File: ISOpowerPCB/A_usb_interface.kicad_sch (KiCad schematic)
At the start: 19 parts

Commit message: modified pcb files
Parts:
- removed C? (x2): 100n, Capacitor_SMD:C_0805_2012Metric_Pad1.18x1.45mm_HandSolder, symbol 000_Capacitor_film_immo:cap_film_0805
- removed C?: 4n7, Capacitor_SMD:C_0805_2012Metric_Pad1.18x1.45mm_HandSolder, symbol 000_Capacitor_film_immo:cap_film_0805
- removed D?: PRTR5V0U2X, Package_TO_SOT_SMD:SOT-143, symbol Power_Protection:PRTR5V0U2X
- removed J?: USB_B_Mini, symbol Connector:USB_B_Mini
- removed R?: 1M, Resistor_SMD:R_0805_2012Metric_Pad1.20x1.40mm_HandSolder, symbol 000_Resistors_Immo:Resistor_0805
- removed TP? (x2): TestPoint, symbol Connector:TestPoint
- removed U?: CH340C, Package_SO:SOIC-16_3.9x9.9mm_P1.27mm, symbol Interface_USB:CH340C
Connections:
- no-connect marks 2 -> 1
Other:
- moved on the sheet: C?, D?, J?, R?, TP?, U?

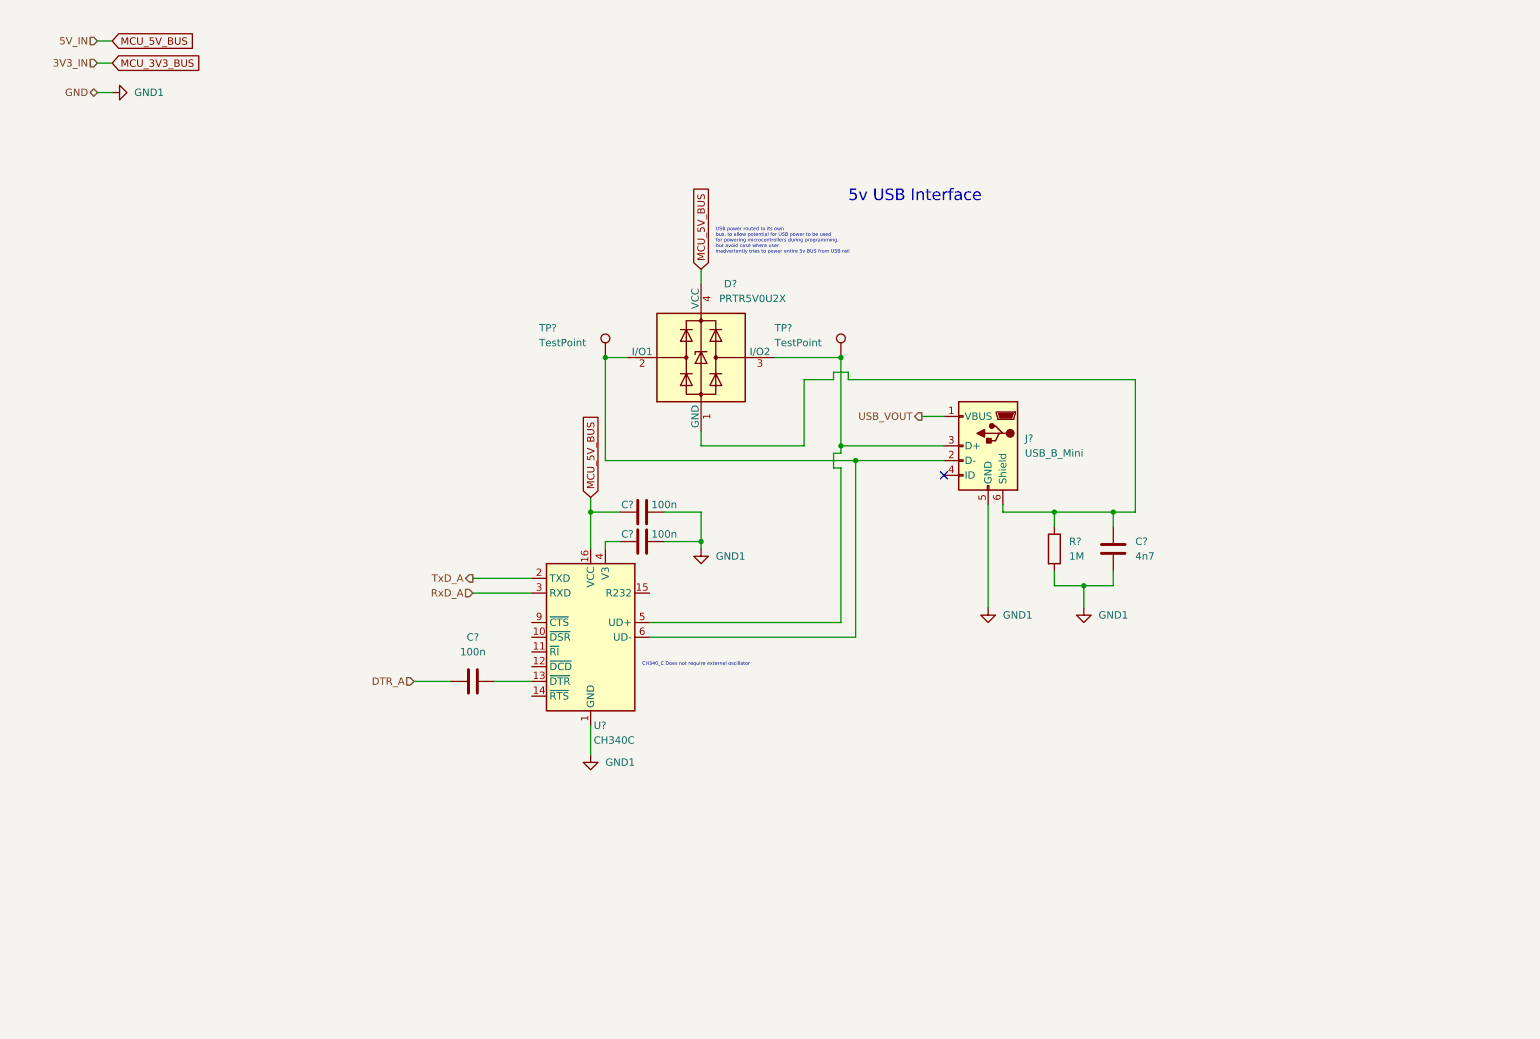
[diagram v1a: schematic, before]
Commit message: Finished initial circuit design
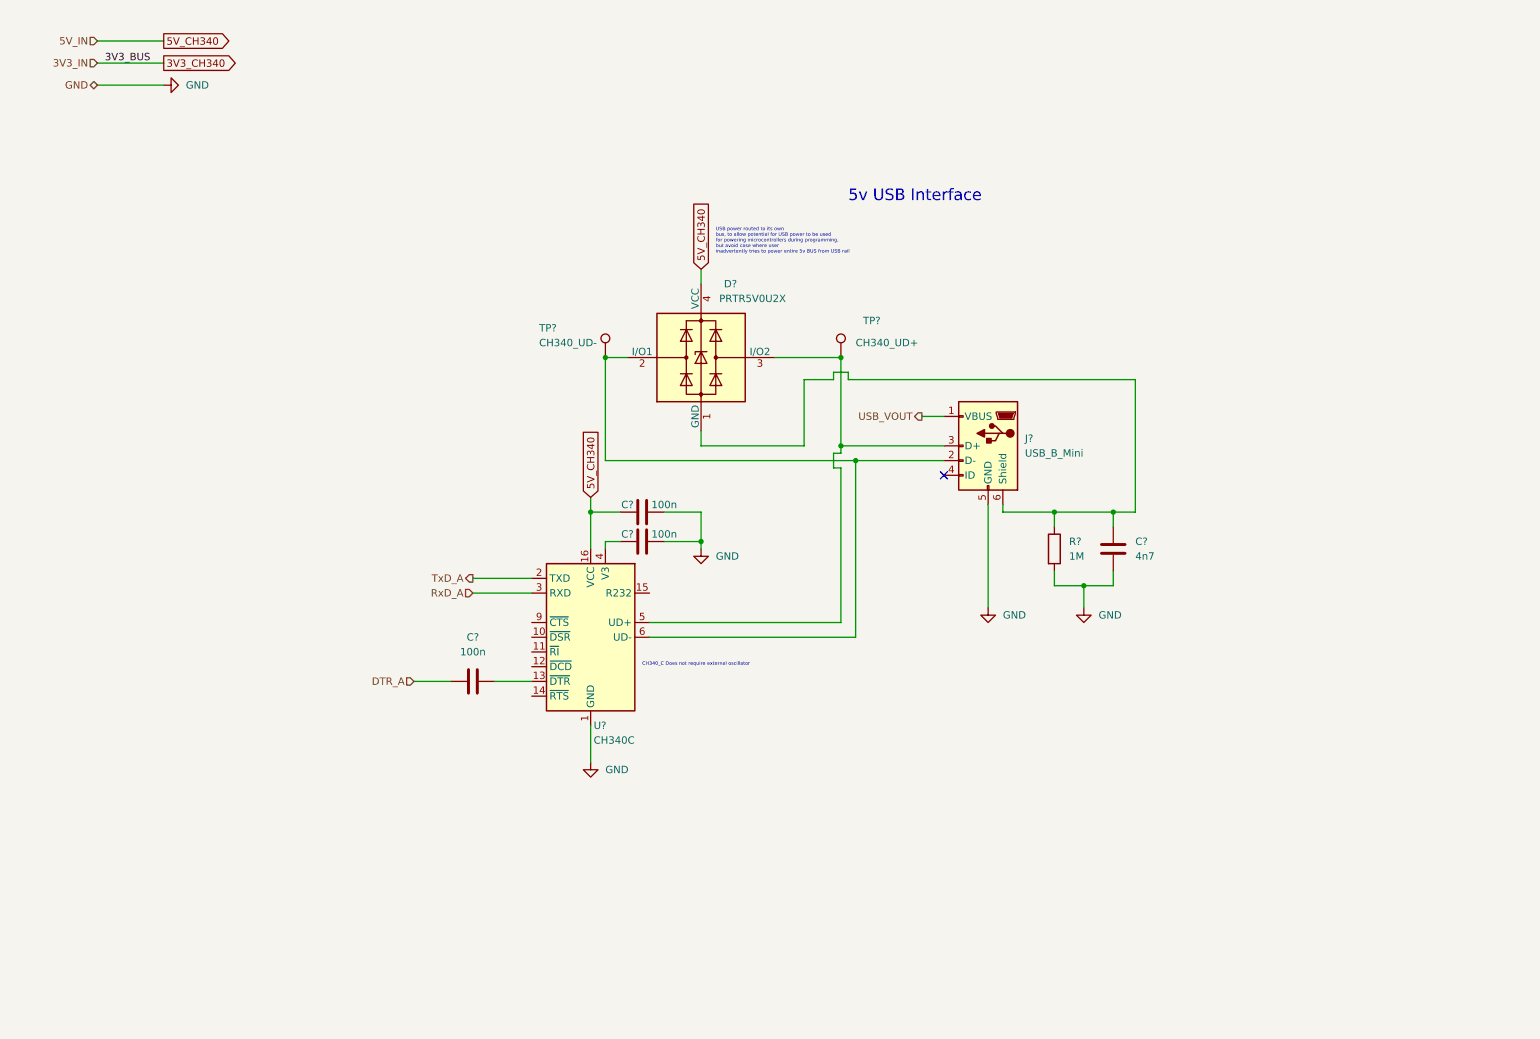
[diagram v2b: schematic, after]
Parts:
- TP?: value TestPoint -> CH340_UD+
- TP?: value TestPoint -> CH340_UD-
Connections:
- net GND1 renamed GND
- net MCU_5V_BUS renamed 5V_CH340

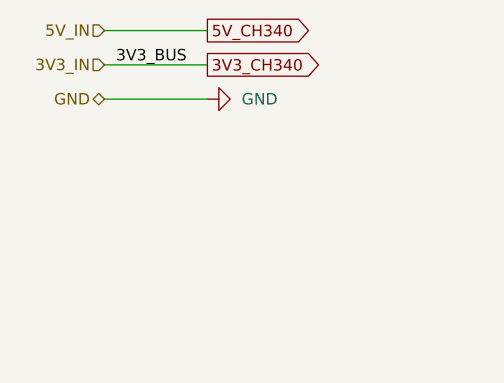
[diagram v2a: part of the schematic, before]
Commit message: Updated as per discussions 26/01/22
# Change Notes

04/02/2022
As per discussion 26/01/22
1. Changed per channel 5v MOSFET switches to MOSFET control of DC/DC module on/off pin - due to failure of MOSFET switching during testing.
2. Added 5v buck converter for independent MCU_5V power bus.
	- Ensured all 5v MCU hardware is powered from common MCU_5V bus.
3. Removed circuit from NC pins on DC/DC modules.
4. Changed ESP32 USB interface to CH340
5. Changed MCU serial logic level converters from MOSFET to IC - TXS0102DCT
	- TODO: OE pin now requires low signal untill DC/DC supply is stable - Does it? Can it just be tied to 5v bus with a large capacitor? Does it need MCU to hold pin low untill 5V_BUS is stable?
6. Removed redundent 3V3_IN to power distribution page.
	- Rechecked all sheets for redundent pins, it won't impact drawing traces, but it will impact readability.
7. Added Mechanical layer as hirarchical sheet.
8. Moved voltage monitoring circuits to hirarchical sheet
9. Added voltage monitoring with TL431DBZ to 12V_BUS
10. Automatic shutoff circuit removed, as this would prevent the DC/DC module from powering on. Instead moved to AtMega328p digital inputs
and microcontroller will control shutdown of DC/DC supply if out of spec voltage detected.
		- This is a severe limitation compared to the specification, and this also does not prevent damage to devices on 5V_BUS if voltage is pulled high, for example to 12v due to user error.
		- TODO: Add independent overvoltage protection to 5V_BUS? 		[Zener Diode Overvoltage Protection - Sparkfun](https://www.rs-online.com/designspark/how-does-zener-diode-do-overvoltage-protection-in-circuit#:~:text=In%20order%20to%20protect%20the,flow%20in%20the%20reverse%20direction).
11. Changed logic level conversion for 12v outputs to 12v drive circuit. [12v drive circuit](https://forum.arduino.cc/t/easiest-way-of-driving-amplifying-from-5v-to-12v/123290)
12. Added proto pin connections for ESP MCU.
13. Changed 20v Zener in reverse vol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
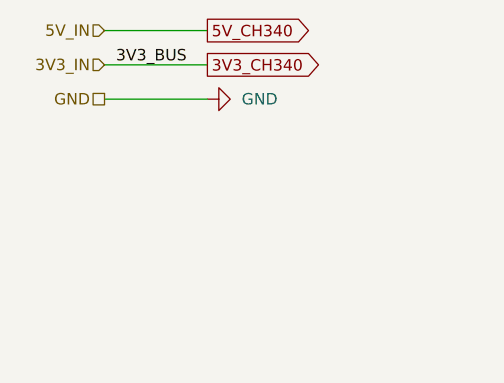
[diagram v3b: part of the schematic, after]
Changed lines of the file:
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@@
     (effects (font (size 1.27 1.27)) (justify right))
   )
-  (hierarchical_label "GND" (shape bidirectional) (at 27.94 30.48 180)
+  (hierarchical_label "GND" (shape passive) (at 27.94 30.48 180)
     (effects (font (size 1.27 1.27)) (justify right))
   )

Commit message: messing around with libraries
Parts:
- C22, C23, C24, C25: renamed from C?; symbol 000_Capacitor_film_immo:cap_film_0805 -> 000_Capacitor_FIlm_Immo:cap_film_0805
- gave numbers to parts that had none: 6
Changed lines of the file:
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@@
     (effects (font (size 1.27 1.27)) (justify right))
   )
-  (symbol (lib_id "000_Capacitor_film_immo:cap_film_0805") (at 92.71 133.35 90) (unit 1)
-    (in_bom yes) (on_board yes) (fields_autoplaced)
-    (property "Reference" "C?" (id 0) (at 92.71 125.73 90))
+  (symbol (lib_id "000_Capacitor_FIlm_Immo:cap_film_0805") (at 92.71 133.35 90) (unit 1)
+    (in_bom yes) (on_board yes) (fields_autoplaced)
+    (property "Reference" "C22" (id 0) (at 92.71 125.73 90))
     (property "Value" "100n" (id 1) (at 92.71 128.27 90))
     (property "Footprint" "Capacitor_SMD:C_0805_2012Metric_Pad1.18x1.45mm_HandSolder" (id 2) (at 102.87 132.08 0)
@@
   (symbol (lib_id "power:GND") (at 181.61 120.65 0) (unit 1)
     (in_bom yes) (on_board yes) (fields_autoplaced)
-    (property "Reference" "#PWR?" (id 0) (at 181.61 127 0)
+    (property "Reference" "#PWR072" (id 0) (at 181.61 127 0)
       (effects (font (size 1.27 1.27)) hide)
     )
@@
     (pin "1")
   )
-  (symbol (lib_id "000_Capacitor_film_immo:cap_film_0805") (at 121.92 109.22 90) (unit 1)
-    (in_bom yes) (on_board yes)
-    (property "Reference" "C?" (id 0) (at 119.38 107.95 90))
+  (symbol (lib_id "000_Capacitor_FIlm_Immo:cap_film_0805") (at 121.92 109.22 90) (unit 1)
+    (in_bom yes) (on_board yes)
+    (property "Reference" "C24" (id 0) (at 119.38 107.95 90))
     (property "Value" "100n" (id 1) (at 125.73 107.95 90))
     (property "Footprint" "Capacitor_SMD:C_0805_2012Metric_Pad1.18x1.45mm_HandSolder" (id 2) (at 132.08 107.95 0)
@@
   (symbol (lib_id "Connector:TestPoint") (at 156.21 77.47 0) (unit 1)
     (in_bom yes) (on_board yes)
-    (property "Reference" "TP?" (id 0) (at 160.02 71.12 0)
+    (property "Reference" "TP8" (id 0) (at 160.02 71.12 0)
       (effects (font (size 1.27 1.27)) (justify left))
     )
@@
   (symbol (lib_id "Power_Protection:PRTR5V0U2X") (at 132.08 77.47 0) (unit 1)
     (in_bom yes) (on_board yes)
-    (property "Reference" "D?" (id 0) (at 137.16 64.77 0))
+    (property "Reference" "D4" (id 0) (at 137.16 64.77 0))
     (property "Value" "PRTR5V0U2X" (id 1) (at 140.97 67.31 0))
     (property "Footprint" "Package_TO_SOT_SMD:SOT-143" (id 2) (at 133.604 77.47 0)
@@
   (symbol (lib_id "power:GND") (at 113.03 147.32 0) (unit 1)
     (in_bom yes) (on_board yes) (fields_autoplaced)
-    (property "Reference" "#PWR?" (id 0) (at 113.03 153.67 0)
+    (property "Reference" "#PWR070" (id 0) (at 113.03 153.67 0)
       (effects (font (size 1.27 1.27)) hide)
     )
@@
   (symbol (lib_id "power:GND") (at 198.12 120.65 0) (unit 1)
     (in_bom yes) (on_board yes) (fields_autoplaced)
-    (property "Reference" "#PWR?" (id 0) (at 198.12 127 0)
+    (property "Reference" "#PWR073" (id 0) (at 198.12 127 0)
       (effects (font (size 1.27 1.27)) hide)
     )
@@
   (symbol (lib_id "000_Resistors_Immo:Resistor_0805") (at 193.04 110.49 0) (unit 1)
     (in_bom yes) (on_board yes)
-    (property "Reference" "R?" (id 0) (at 195.58 109.2199 0)
+    (property "Reference" "R8" (id 0) (at 195.58 109.2199 0)
       (effects (font (size 1.27 1.27)) (justify left))
     )
@@
   (symbol (lib_id "power:GND") (at 132.08 110.49 0) (unit 1)
     (in_bom yes) (on_board yes) (fields_autoplaced)
-    (property "Reference" "#PWR?" (id 0) (at 132.08 116.84 0)
+    (property "Reference" "#PWR071" (id 0) (at 132.08 116.84 0)
       (effects (font (size 1.27 1.27)) hide)
     )
@@
   (symbol (lib_id "Connector:TestPoint") (at 115.57 77.47 0) (unit 1)
     (in_bom yes) (on_board yes)
-    (property "Reference" "TP?" (id 0) (at 104.14 72.39 0)
+    (property "Reference" "TP7" (id 0) (at 104.14 72.39 0)
       (effects (font (size 1.27 1.27)) (justify left))
     )
@@
   (symbol (lib_id "Connector:USB_B_Mini") (at 181.61 92.71 0) (mirror y) (unit 1)
     (in_bom yes) (on_board yes) (fields_autoplaced)
-    (property "Reference" "J?" (id 0) (at 187.96 91.4399 0)
+    (property "Reference" "J19" (id 0) (at 187.96 91.4399 0)
       (effects (font (size 1.27 1.27)) (justify right))
     )
@@
     (pin "6")
   )
-  (symbol (lib_id "000_Capacitor_film_immo:cap_film_0805") (at 203.2 110.49 180) (unit 1)
-    (in_bom yes) (on_board yes) (fields_autoplaced)
-    (property "Reference" "C?" (id 0) (at 207.01 109.2199 0)
+  (symbol (lib_id "000_Capacitor_FIlm_Immo:cap_film_0805") (at 203.2 110.49 180) (unit 1)
+    (in_bom yes) (on_board yes) (fields_autoplaced)
+    (property "Reference" "C25" (id 0) (at 207.01 109.2199 0)
       (effects (font (size 1.27 1.27)) (justify right))
     )
@@
   (symbol (lib_id "Interface_USB:CH340C") (at 113.03 125.73 0) (mirror y) (unit 1)
     (in_bom yes) (on_board yes) (fields_autoplaced)
-    (property "Reference" "U?" (id 0) (at 113.5506 140.97 0)
+    (property "Reference" "U12" (id 0) (at 113.5506 140.97 0)
       (effects (font (size 1.27 1.27)) (justify right))
     )
@@
     (pin "9")
   )
-  (symbol (lib_id "000_Capacitor_film_immo:cap_film_0805") (at 121.92 104.14 90) (unit 1)
-    (in_bom yes) (on_board yes)
-    (property "Reference" "C?" (id 0) (at 119.38 102.87 90))
+  (symbol (lib_id "000_Capacitor_FIlm_Immo:cap_film_0805") (at 121.92 104.14 90) (unit 1)
+    (in_bom yes) (on_board yes)
+    (property "Reference" "C23" (id 0) (at 119.38 102.87 90))
     (property "Value" "100n" (id 1) (at 125.73 102.87 90))
     (property "Footprint" "Capacitor_SMD:C_0805_2012Metric_Pad1.18x1.45mm_HandSolder" (id 2) (at 132.08 102.87 0)
@@
   (symbol (lib_id "power:GND") (at 39.37 30.48 90) (unit 1)
     (in_bom yes) (on_board yes) (fields_autoplaced)
-    (property "Reference" "#PWR?" (id 0) (at 45.72 30.48 0)
-      (effects (font (size 1.27 1.27)) hide)
-    )
+    (property "Reference" "#PWR069" (id 0) (at 45.72 30.48 0)
+      (effects (font (size 1.27 1.27)) hide)
+    )

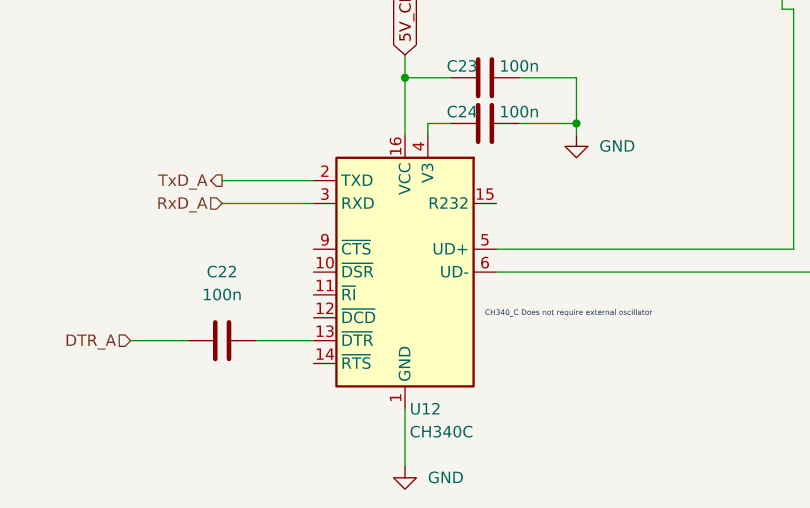
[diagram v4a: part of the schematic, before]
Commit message: adding logic for fault indication
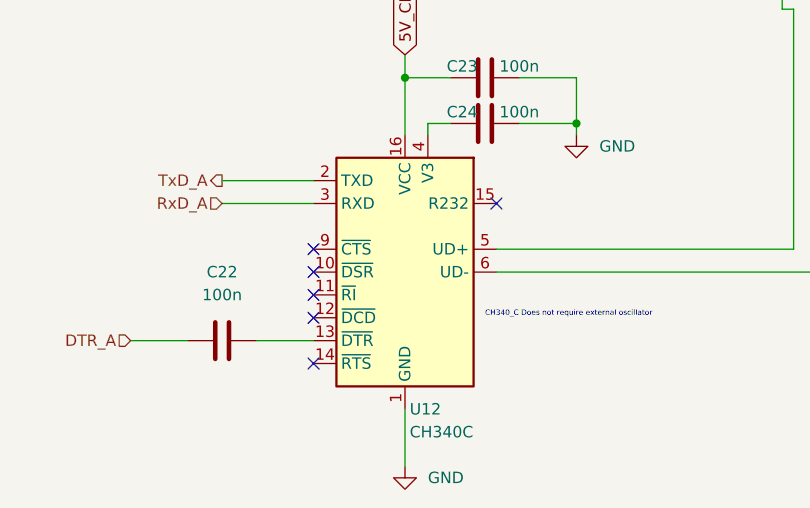
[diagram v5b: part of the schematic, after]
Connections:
- no-connect marks 1 -> 7
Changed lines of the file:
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@@
   (junction (at 156.21 92.71) (diameter 0) (color 0 0 0 0)
   )
+  (no_connect (at 102.87 128.27))
+  (no_connect (at 102.87 130.81))
+  (no_connect (at 123.19 118.11))
+  (no_connect (at 102.87 125.73))
+  (no_connect (at 102.87 135.89))
+  (no_connect (at 102.87 123.19))
   (no_connect (at 173.99 97.79))
   (wire (pts (xy 144.78 77.47) (xy 156.21 77.47))

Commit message: fixed most electrical rules check violations
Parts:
- C22, C23, C24, C25: symbol 000_Capacitor_FIlm_Immo:cap_film_0805 -> 000_Capacitor_Film_Immo:cap_film_0805
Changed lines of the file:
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@@
     (effects (font (size 1.27 1.27)) (justify right))
   )
-  (symbol (lib_id "000_Capacitor_FIlm_Immo:cap_film_0805") (at 92.71 133.35 90) (unit 1)
+  (symbol (lib_id "000_Capacitor_Film_Immo:cap_film_0805") (at 92.71 133.35 90) (unit 1)
     (in_bom yes) (on_board yes) (fields_autoplaced)
     (property "Reference" "C22" (id 0) (at 92.71 125.73 90))
@@
     (pin "1")
   )
-  (symbol (lib_id "000_Capacitor_FIlm_Immo:cap_film_0805") (at 121.92 109.22 90) (unit 1)
+  (symbol (lib_id "000_Capacitor_Film_Immo:cap_film_0805") (at 121.92 109.22 90) (unit 1)
     (in_bom yes) (on_board yes)
     (property "Reference" "C24" (id 0) (at 119.38 107.95 90))
@@
     (pin "6")
   )
-  (symbol (lib_id "000_Capacitor_FIlm_Immo:cap_film_0805") (at 203.2 110.49 180) (unit 1)
+  (symbol (lib_id "000_Capacitor_Film_Immo:cap_film_0805") (at 203.2 110.49 180) (unit 1)
     (in_bom yes) (on_board yes) (fields_autoplaced)
     (property "Reference" "C25" (id 0) (at 207.01 109.2199 0)
@@
     (pin "9")
   )
-  (symbol (lib_id "000_Capacitor_FIlm_Immo:cap_film_0805") (at 121.92 104.14 90) (unit 1)
+  (symbol (lib_id "000_Capacitor_Film_Immo:cap_film_0805") (at 121.92 104.14 90) (unit 1)
     (in_bom yes) (on_board yes)
     (property "Reference" "C23" (id 0) (at 119.38 102.87 90))
